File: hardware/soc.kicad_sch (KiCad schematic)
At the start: 4 parts, among them U16 MPFS025T-FCVG484E, U4 MPFS025T-FCVG484E

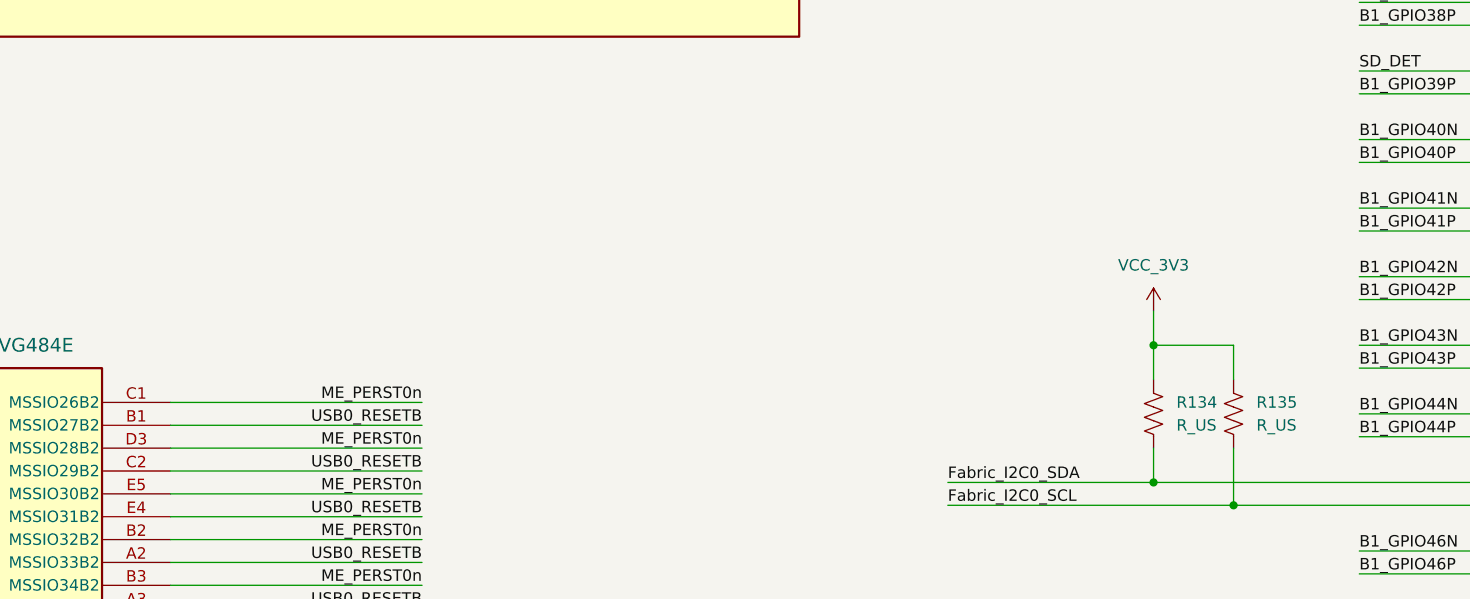
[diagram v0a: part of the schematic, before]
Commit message: assigned footprints of resistors and some capacitors
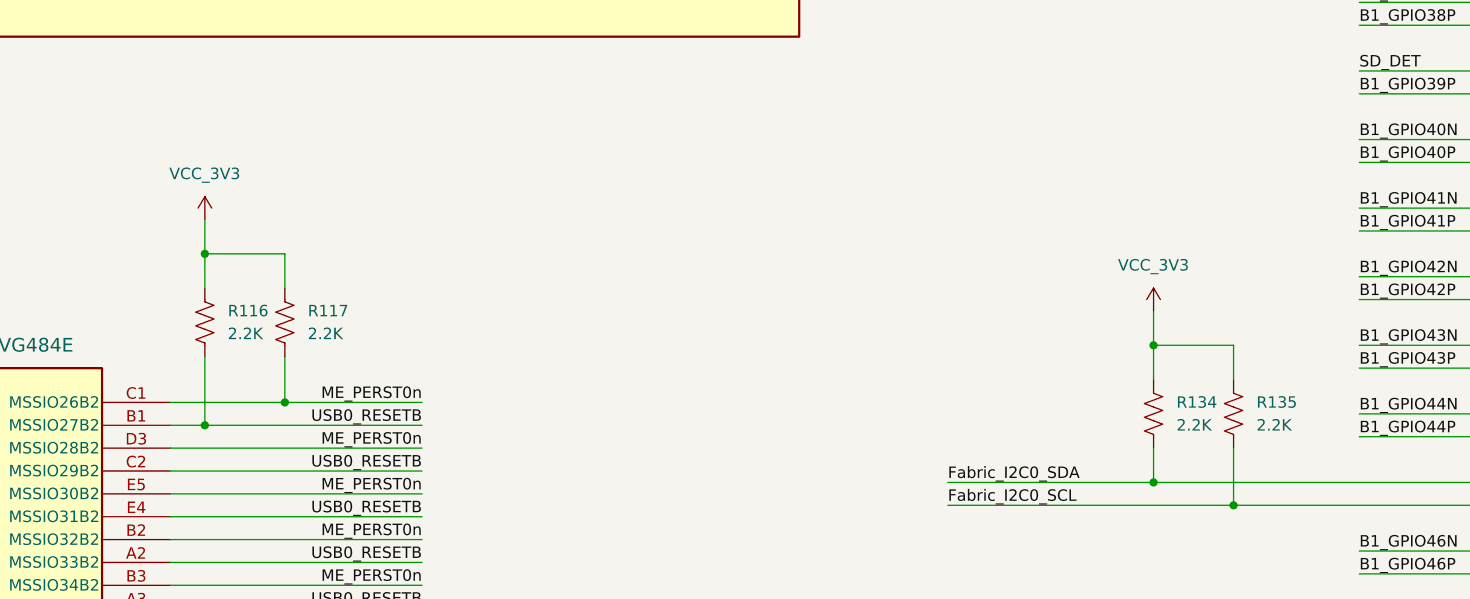
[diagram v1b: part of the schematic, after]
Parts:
- added R116, R117: 2.2K, payload_footprints:RESC1005X40N, symbol Device:R_US
- R134, R135: value R_US -> 2.2K; footprint (none) -> payload_footprints:RESC1005X40N
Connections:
- net ME_PERST0n: now also R117.2
- net USB0_RESETB: now also R116.2
- net VCC_3V3: now also R116.1, R117.1

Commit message: renamed and assigned some connections concerning FPGA banks, sensors, interfaces
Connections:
- net ME_PERST0n: no longer R117.2, U16.B2 (MSSIO32B2), U16.B3 (MSSIO34B2), U16.C1 (MSSIO26B2), U16.D3 (MSSIO28B2), U16.E3 (MSSIO36B2), U16.E5 (MSSIO30B2)
- net USB0_RESETB: no longer R116.2, U16.A2 (MSSIO33B2), U16.A3 (MSSIO35B2), U16.B1 (MSSIO27B2), U16.C2 (MSSIO29B2), U16.D4 (MSSIO37B2), U16.E4 (MSSIO31B2)
- new net ADC_CSn: U16.E4 (MSSIO31B2)
- new net ADC_IROn: U16.B3 (MSSIO34B2)
- new net ADC_MISO: U16.A2 (MSSIO33B2)
- new net ADC_MOSI: U16.B2 (MSSIO32B2)
- new net ADC_SCK: U16.E5 (MSSIO30B2)
- new net I2C1_SCL: R117.2, U16.C1 (MSSIO26B2)
- new net I2C1_SDA: R116.2, U16.B1 (MSSIO27B2)
- new net PHY_MDC: U16.A3 (MSSIO35B2)
- new net PHY_MDIO: U16.E3 (MSSIO36B2)
- new net UART0_RXD: U16.D3 (MSSIO28B2)
- new net UART0_TXD: U16.C2 (MSSIO29B2)
- new net USB0_OCn: U16.D4 (MSSIO37B2)
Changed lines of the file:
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@@
 		)
 	)
-	(label "USB0_RESETB"
+	(label "I2C1_SDA"
 		(at 124.46 207.01 180)
 		(effects
@@
 		)
 	)
-	(label "ME_PERST0n"
+	(label "ADC_MOSI"
 		(at 124.46 219.71 180)
 		(effects
@@
 		)
 	)
-	(label "ME_PERST0n"
+	(label "I2C1_SCL"
 		(at 124.46 204.47 180)
 		(effects
@@
 		)
 	)
-	(label "USB0_RESETB"
+	(label "UART0_TXD"
 		(at 124.46 212.09 180)
 		(effects
@@
 		)
 	)
-	(label "ME_PERST0n"
+	(label "UART0_RXD"
 		(at 124.46 209.55 180)
 		(effects
@@
 		)
 	)
-	(label "USB0_RESETB"
+	(label "ADC_CSn"
 		(at 124.46 217.17 180)
 		(effects
@@
 		)
 	)
-	(label "USB0_RESETB"
+	(label "USB0_OCn"
 		(at 124.46 232.41 180)
 		(effects
@@
 		)
 	)
-	(label "USB0_RESETB"
+	(label "ADC_MISO"
 		(at 124.46 222.25 180)
 		(effects
@@
 		)
 	)
-	(label "ME_PERST0n"
+	(label "ADC_IROn"
 		(at 124.46 224.79 180)
 		(effects
@@
 		)
 	)
-	(label "USB0_RESETB"
+	(label "PHY_MDC"
 		(at 124.46 227.33 180)
 		(effects
@@
 		)
 	)
-	(label "ME_PERST0n"
+	(label "ADC_SCK"
 		(at 124.46 214.63 180)
 		(effects
@@
 		)
 	)
-	(label "ME_PERST0n"
+	(label "PHY_MDIO"
 		(at 124.46 229.87 180)
 		(effects
